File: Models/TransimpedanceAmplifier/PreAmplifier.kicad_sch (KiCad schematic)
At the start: 10 parts, among them U5 AD8615AUJZ-R2

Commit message: Finished for today
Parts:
- C1, C2, C3, C4: Purchase Link (none) -> https://www.digikey.com/en/products/detail/murata-electroni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
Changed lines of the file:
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@@
 			)
 		)
-		(property "Purchase Link" ""
+		(property "Purchase Link" "https://www.digikey.com/en/products/detail/murata-electronics/GRT188R61H105KE13D/5416752"
 			(at 157.48 66.04 0)
 			(effects
@@
 			)
 		)
-		(property "Purchase Link" ""
+		(property "Purchase Link" "https://www.digikey.com/en/products/detail/murata-electronics/GRT188R61H105KE13D/5416752"
 			(at 157.48 95.25 0)
 			(effects
@@
 			)
 		)
-		(property "Purchase Link" ""
+		(property "Purchase Link" "https://www.digikey.com/en/products/detail/murata-electronics/GRM21BR61E106KA73K/4905532"
 			(at 177.8 66.04 0)
 			(effects
@@
 			)
 		)
-		(property "Purchase Link" ""
+		(property "Purchase Link" "https://www.digikey.com/en/products/detail/murata-electronics/GRM21BR61E106KA73K/4905532"
 			(at 177.8 95.25 0)
 			(effects

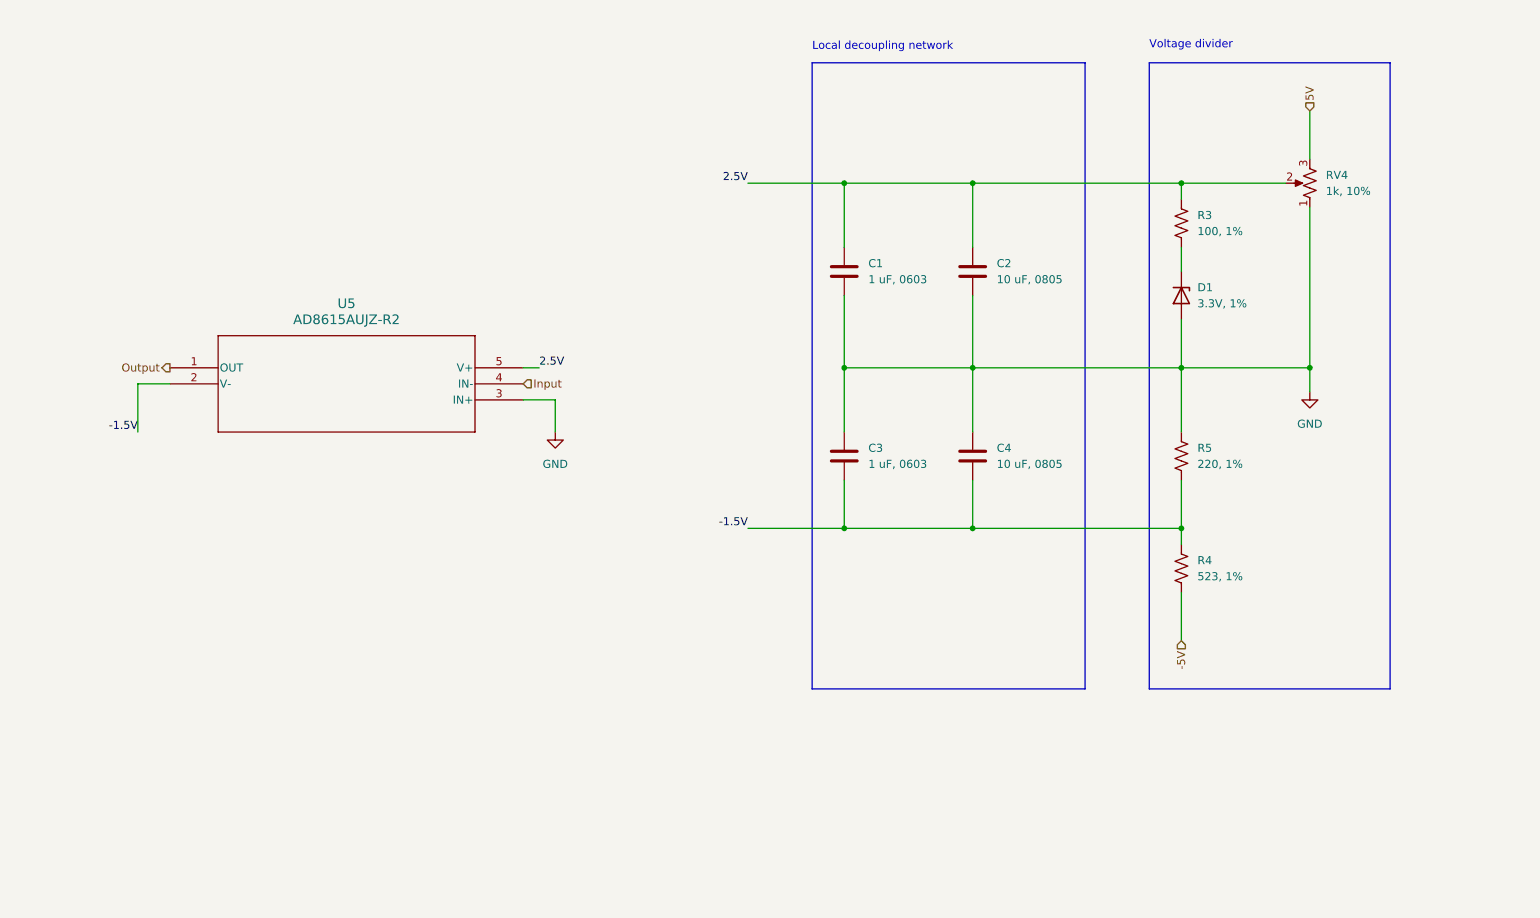
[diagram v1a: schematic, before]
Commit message: Fixed the 3.3V Zener
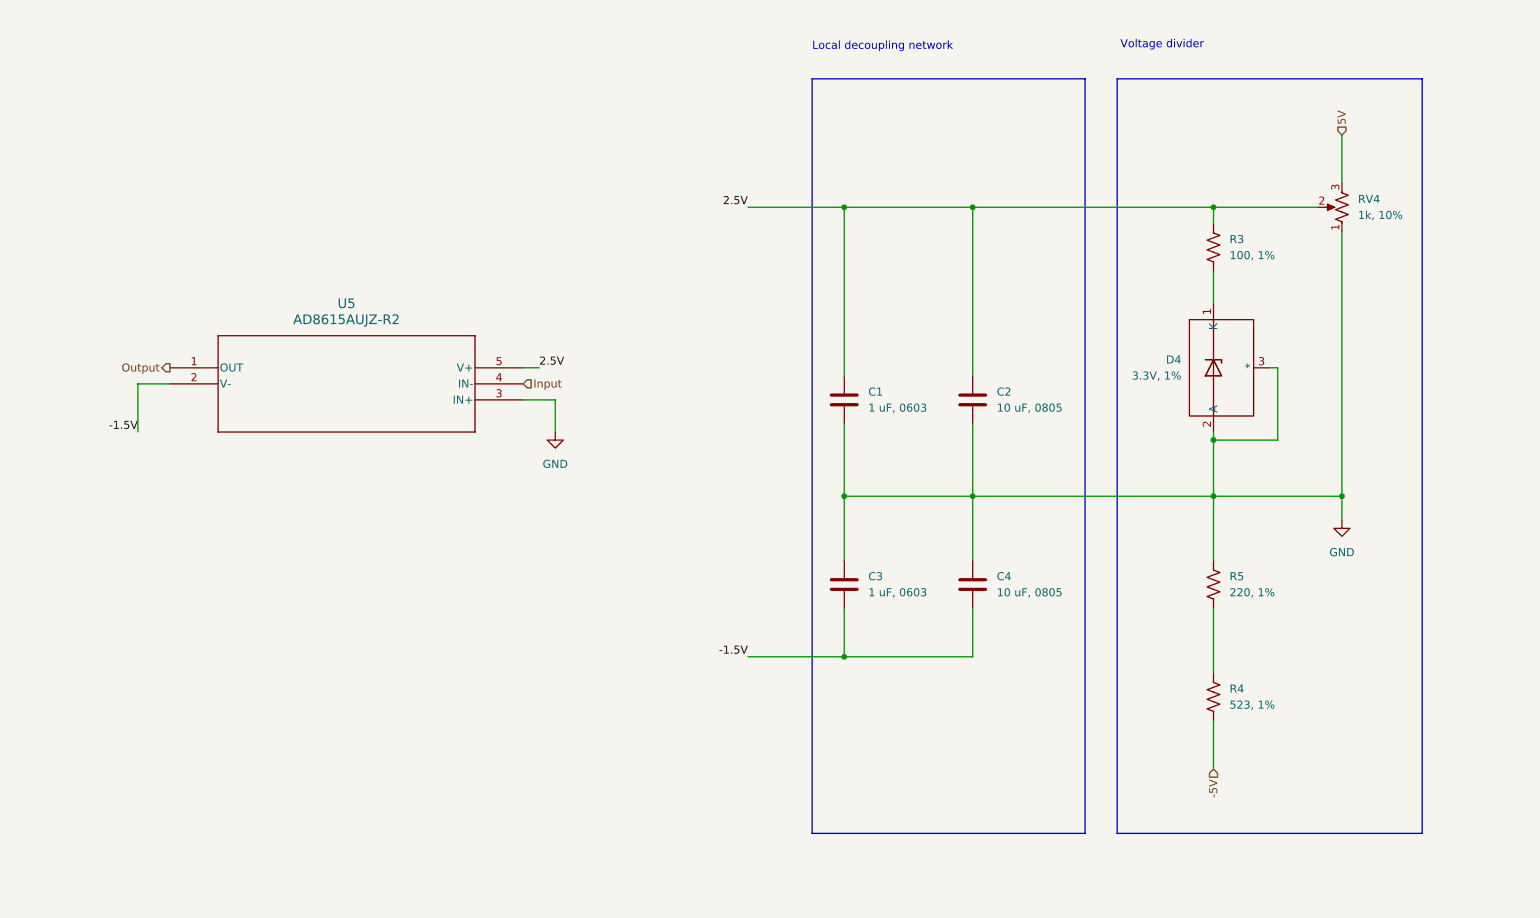
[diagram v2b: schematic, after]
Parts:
- removed D1: 3.3V, 1%, symbol Device:D_Zener
- added D4: 3.3V, 1%, symbol Custom:D_Zener
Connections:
- net -1.5V: no longer R4.1, R5.2
- net GND: now also D4.2 (A), D4.3 (*)
- net at R3.2: now also D4.1 (K)
- new net: R4.1, R5.2
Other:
- moved on the sheet: C1, C2, C3, C4, R3, R4, R5, RV4

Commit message: Save progress
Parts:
- removed D4: 3.3V, 1%, symbol Custom:D_Zener
- added D1: 3.3V, 1%, symbol Custom:D_Zener
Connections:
- net GND: now also D1.2 (A), D1.3 (*)
- net at R3.2: now also D1.1 (K)

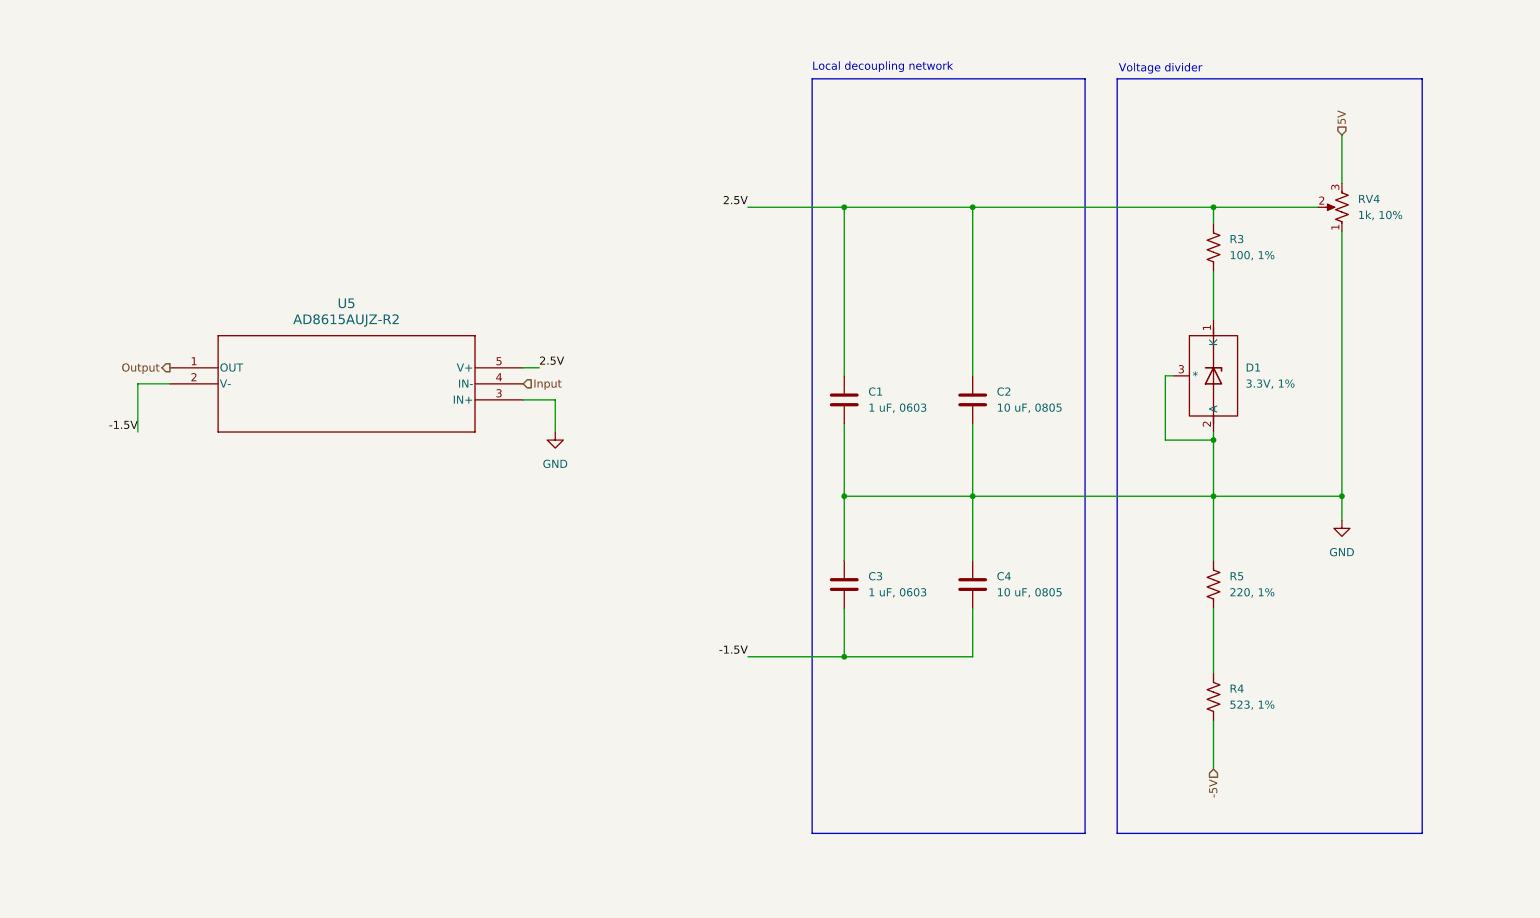
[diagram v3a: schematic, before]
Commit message: This should be all of the pin headers
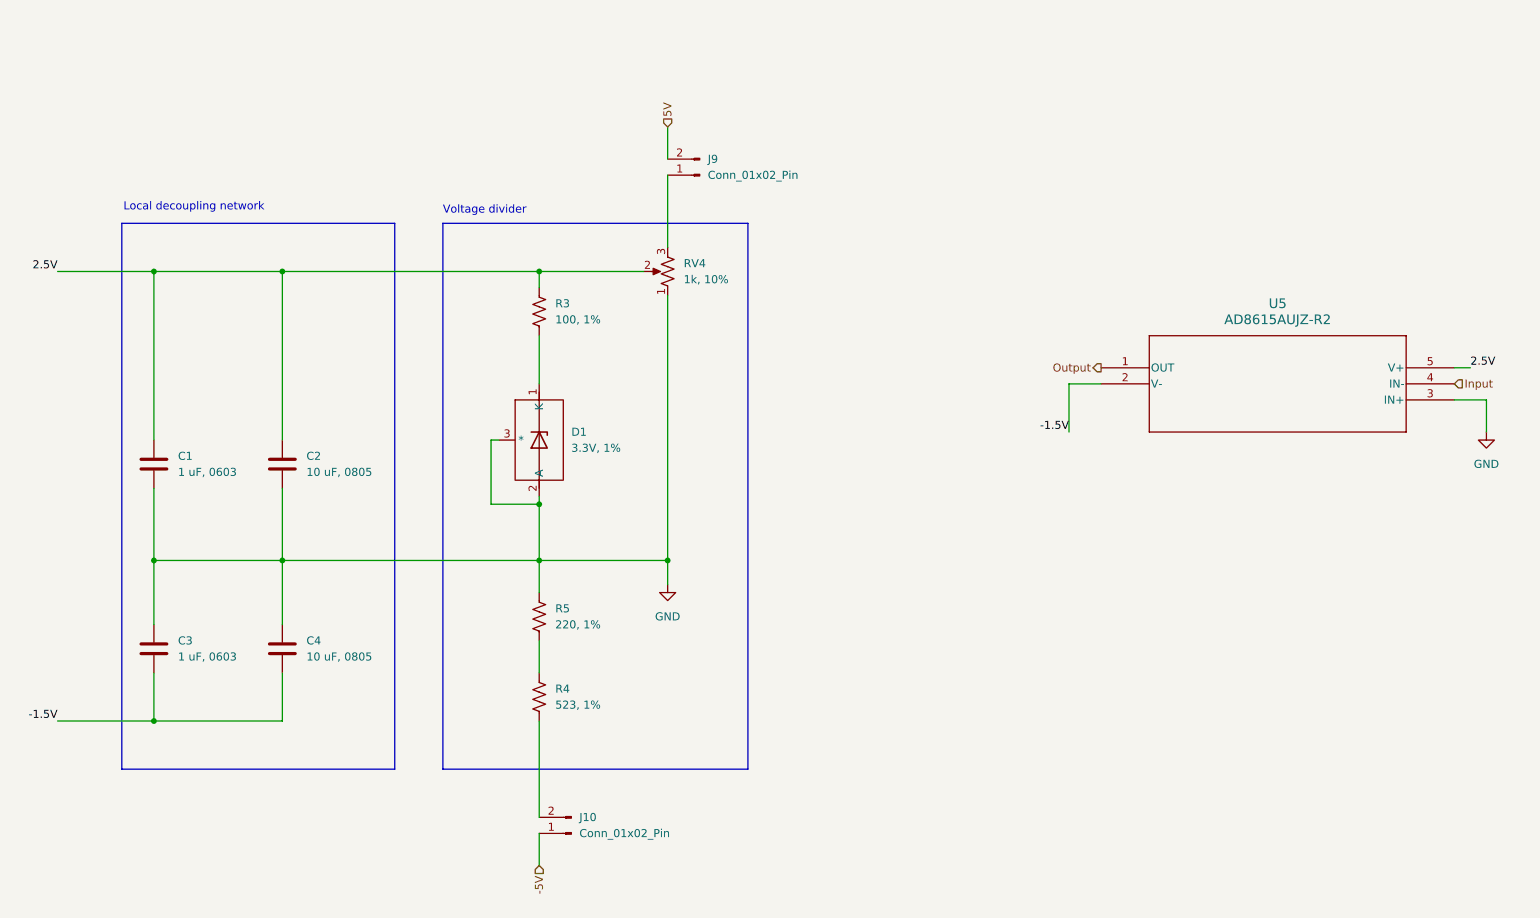
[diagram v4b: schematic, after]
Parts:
- added J10, J9: Conn_01x02_Pin, symbol Connector:Conn_01x02_Pin
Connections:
- net -5V: now also J10.1 (Pin_1); no longer R4.2
- net 5V: now also J9.2 (Pin_2); no longer RV4.3
- new net: J9.1 (Pin_1), RV4.3
- new net: J10.2 (Pin_2), R4.2
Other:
- moved on the sheet: C1, C2, C3, C4, D1, R3, R4, R5, RV4, U5

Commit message: Save progress
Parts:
- J10, J9: Purchase Link (none) -> https://www.digikey.com/en/products/detail/sullins-connecto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
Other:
- moved on the sheet: C1, C2, C3, C4, D1, J10, J9, R3, R4, R5, RV4, U5

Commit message: Save progress
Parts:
- U5: footprint UJ_5_ADI -> (none)
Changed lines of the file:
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@@
 			)
 		)
-		(property "Footprint" "UJ_5_ADI"
+		(property "Footprint" ""
 			(at 43.18 81.28 0)
 			(effects

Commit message: Save progress
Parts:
- U5: value AD8615AUJZ-R2 -> AD8615
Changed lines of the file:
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@@
 			)
 		)
-		(property "Value" "AD8615AUJZ-R2"
+		(property "Value" "AD8615"
 			(at 71.12 73.66 0)
 			(effects
